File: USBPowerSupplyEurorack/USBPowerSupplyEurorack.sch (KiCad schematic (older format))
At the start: 19 parts, among them J1 1734366-1, J2 10129381-910001BLF, Q1 Q_PMOS_GSD

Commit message: added footprints with LCSC components
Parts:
- removed L1: 744235601, 744235601, symbol 744235601:744235601
- added L1: ACM4520V-901-2P-T, eec2:TDK-ACM4520V-901-2P-T-0, symbol eec2:ACM4520V-901-2P-T
- C1: footprint (none) -> Capacitor_SMD:C_Elec_8x10.2
- C2: footprint (none) -> Capacitor_SMD:C_1210_3225Metric
- C3, C4: footprint (none) -> Capacitor_SMD:C_1206_3216Metric
- C5, C6: footprint (none) -> Capacitor_SMD:C_Elec_4x5.4
- C7: footprint (none) -> Capacitor_SMD:C_Elec_6.3x5.8
- D2: value P4SMAJ15CA -> SMAJ5.0CA; footprint (none) -> digikey-footprints:DO-214AC
- D3, D4: footprint Diode_THT:D_DO-41_SOD81_P10.16mm_Horizontal -> Diode_SMD:D_SOD-123F
- F1: value 1812L110_16DR -> 1812L110; footprint FUSC4632X125N -> 1812L110_16DR:FUSC4632X125N; Description PTC Resettable Fuse 1.1A(hold) 1.95A(trip) 16VDC 100A 0.8W 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 -> PTC Resettable Fuse 1.1A(hold) 1.95A(trip) 8VDC 100A 0.8W 0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
- J2: footprint HDRV10W67P254_2X5_1270X483X858P -> 10129381-910001BLF:HDRV10W67P254_2X5_1270X483X858P
- R1: value 100 -> 510; footprint (none) -> Resistor_SMD:R_0612_1632Metric
- S1: footprint LP4OA1PBCTR -> LP4OA1PBCTR:LP4OA1PBCTR
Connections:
- net +12V: now also S1.L1 (A_RED)
- net +5V: now also L1.2; no longer R1.2, S1.L1 (A_RED)
- net +Vin: now also L1.4
- net -Vin: now also L1.3
- net 0V: now also R1.2
- net at C1.1, C2.1, C7.1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: now also L1.1
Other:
- moved on the sheet: C1, C2, C7, D2, Q1

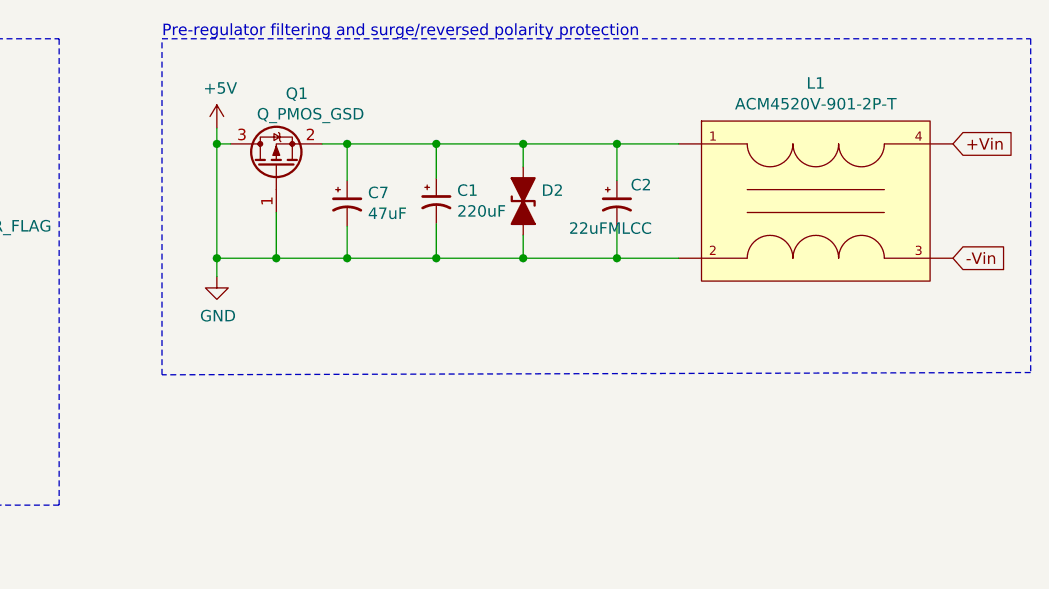
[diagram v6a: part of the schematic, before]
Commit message: changed TVS symbol as footprint was not valid
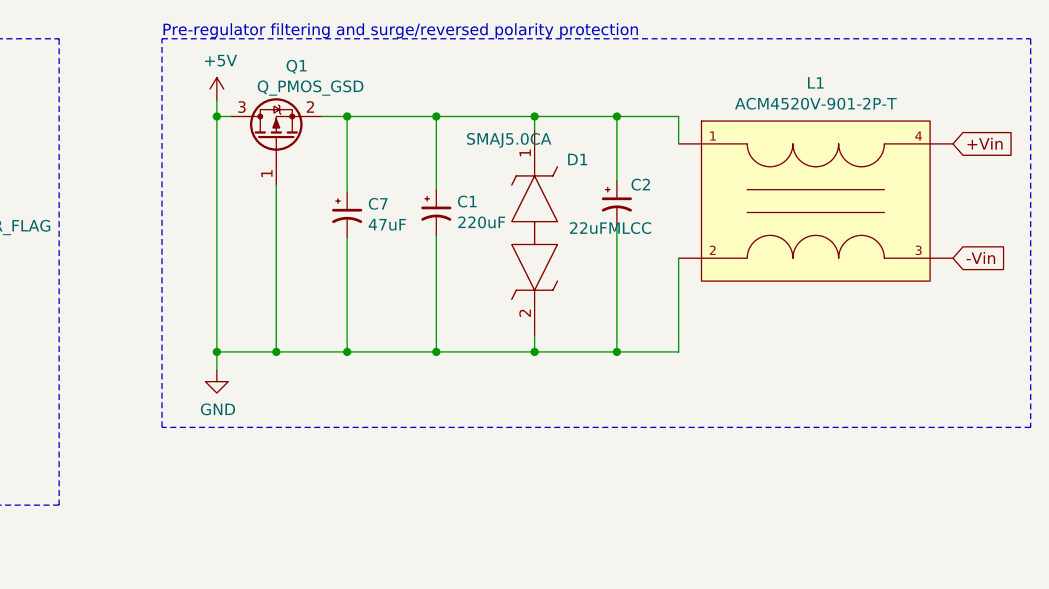
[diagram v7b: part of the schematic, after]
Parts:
- removed D2: SMAJ5.0CA, digikey-footprints:DO-214AC, symbol Device:D_TVS_ALT
- added D1: SMAJ5.0CA, DIONM5026X229N, symbol SMAJ5.0CA:SMAJ5.0CA
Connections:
- net +5V: now also D1.2
- net at C1.1, C2.1, C7.1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: now also D1.1
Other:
- moved on the sheet: C1, C7, Q1
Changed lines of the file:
@@
 L Device:CP1_Small C1
 U 1 1 5FE096E1
-P 8010 1720
-F 0 "C1" H 8101 1766 50  0000 L CNN
-F 1 "220uF" H 8101 1675 50  0000 L CNN
-F 2 "Capacitor_SMD:C_Elec_8x10.2" H 8010 1720 50  0001 C CNN
-F 3 "~" H 8010 1720 50  0001 C CNN
-	1    8010 1720
-	1    0    0    -1
-$EndComp
-$Comp
-L Device:D_TVS_ALT D2
-U 1 1 5FE0A48F
-P 8390 1720
-F 0 "D2" V 8344 1800 50  0000 L CNN
-F 1 "SMAJ5.0CA" V 8435 1800 50  0001 L CNN
-F 2 "digikey-footprints:DO-214AC" H 8390 1720 50  0001 C CNN
-F 3 "~" H 8390 1720 50  0001 C CNN
-	1    8390 1720
-	0    1    1    0
+P 8010 1770
+F 0 "C1" H 8101 1816 50  0000 L CNN
+F 1 "220uF" H 8101 1725 50  0000 L CNN
+F 2 "Capacitor_SMD:C_Elec_8x10.2" H 8010 1770 50  0001 C CNN
+F 3 "~" H 8010 1770 50  0001 C CNN
+	1    8010 1770
+	1    0    0    -1
 $EndComp
 $Comp
@@
 L power:+5V #PWR0106
 U 1 1 5FE2FAE8
-P 7050 1400
-F 0 "#PWR0106" H 7050 1250 50  0001 C CNN
-F 1 "+5V" H 7065 1573 50  0000 C CNN
-F 2 "" H 7050 1400 50  0001 C CNN
-F 3 "" H 7050 1400 50  0001 C CNN
-	1    7050 1400
+P 7050 1280
+F 0 "#PWR0106" H 7050 1130 50  0001 C CNN
+F 1 "+5V" H 7065 1453 50  0000 C CNN
+F 2 "" H 7050 1280 50  0001 C CNN
+F 3 "" H 7050 1280 50  0001 C CNN
+	1    7050 1280
 	1    0    0    -1
 $EndComp
@@
 $EndComp
 Wire Wire Line
-	8800 1830 8800 1970
-Wire Wire Line
-	8800 1630 8800 1470
-Wire Wire Line
-	8390 1570 8390 1470
-Wire Wire Line
-	8390 1470 8800 1470
-Wire Wire Line
-	8390 1870 8390 1970
-Wire Wire Line
-	8390 1970 8800 1970
-Wire Wire Line
-	8010 1620 8010 1470
-Wire Wire Line
-	8010 1470 8390 1470
-Connection ~ 8390 1470
-Wire Wire Line
-	8010 1820 8010 1970
-Wire Wire Line
-	8010 1970 8390 1970
-Connection ~ 8390 1970
+	8010 1670 8010 1350
+Wire Wire Line
+	8010 1870 8010 2380
 $Comp
 L power:GND #PWR0107
 U 1 1 5FE34916
-P 7050 2050
-F 0 "#PWR0107" H 7050 1800 50  0001 C CNN
-F 1 "GND" H 7055 1877 50  0000 C CNN
-F 2 "" H 7050 2050 50  0001 C CNN
-F 3 "" H 7050 2050 50  0001 C CNN
-	1    7050 2050
-	1    0    0    -1
-$EndComp
-Connection ~ 8010 1970
+P 7050 2460
+F 0 "#PWR0107" H 7050 2210 50  0001 C CNN
+F 1 "GND" H 7055 2287 50  0000 C CNN
+F 2 "" H 7050 2460 50  0001 C CNN
+F 3 "" H 7050 2460 50  0001 C CNN
+	1    7050 2460
+	1    0    0    -1
+$EndComp
+Connection ~ 8010 2380
 Wire Wire Line
 	2480 1490 2560 1490
 Wire Wire Line
 	2560 1490 2560 1440
-Connection ~ 8010 1470
+Connection ~ 8010 1350
 Text GLabel 10270 1470 2    50   Input ~ 0
 +Vin
@@
 L Device:CP1_Small C7
 U 1 1 5FE548E0
-P 7620 1730
-F 0 "C7" H 7711 1776 50  0000 L CNN
-F 1 "47uF" H 7711 1685 50  0000 L CNN
-F 2 "Capacitor_SMD:C_Elec_6.3x5.8" H 7620 1730 50  0001 C CNN
-F 3 "~" H 7620 1730 50  0001 C CNN
-	1    7620 1730
+P 7620 1780
+F 0 "C7" H 7711 1826 50  0000 L CNN
+F 1 "47uF" H 7711 1735 50  0000 L CNN
+F 2 "Capacitor_SMD:C_Elec_6.3x5.8" H 7620 1780 50  0001 C CNN
+F 3 "~" H 7620 1780 50  0001 C CNN
+	1    7620 1780
 	1    0    0    -1
 $EndComp
@@
 	4990 5650 4820 5650
 Wire Wire Line
-	8010 1470 7620 1470
-Wire Wire Line
-	7620 1470 7620 1630
-Wire Wire Line
-	7620 1830 7620 1970
-Wire Wire Line
-	7620 1970 8010 1970
-Connection ~ 7620 1970
-Connection ~ 7620 1470
+	8010 1350 7620 1350
+Wire Wire Line
+	7620 1350 7620 1680
+Wire Wire Line
+	7620 1880 7620 2380
+Wire Wire Line
+	7620 2380 8010 2380
+Connection ~ 7620 2380
+Connection ~ 7620 1350
 Wire Notes Line
 	6810 1010 10610 1010
 Wire Notes Line
-	10610 1010 10610 2470
-Wire Notes Line
-	10610 2470 6810 2480
-Wire Notes Line
-	6810 2480 6810 1010
+	10610 1010 10610 2710
+Wire Notes Line
+	10610 2710 6810 2710
+Wire Notes Line
+	6810 2710 6810 1010
 Text Notes 6810 1010 0    50   ~ 0
 Pre-regulator filtering and surge/reversed polarity protection
@@
 L Device:Q_PMOS_GSD Q1
 U 1 1 5FE39F03
-P 7310 1570
-F 0 "Q1" V 7630 1480 50  0000 C CNN
-F 1 "Q_PMOS_GSD" V 7540 1420 50  0000 C CNN
-F 2 "digikey-footprints:SOT-23-3" H 7510 1670 50  0001 C CNN
-F 3 "https://www.mouser.fr/datasheet/2/916/PMV240SP-1919536.pdf" H 7310 1570 50  0001 C CNN
-	1    7310 1570
+P 7310 1450
+F 0 "Q1" V 7630 1360 50  0000 C CNN
+F 1 "Q_PMOS_GSD" V 7540 1300 50  0000 C CNN
+F 2 "digikey-footprints:SOT-23-3" H 7510 1550 50  0001 C CNN
+F 3 "https://www.mouser.fr/datasheet/2/916/PMV240SP-1919536.pdf" H 7310 1450 50  0001 C CNN
+	1    7310 1450
 	0    -1   -1   0
 $EndComp
 Wire Wire Line
-	7620 1470 7510 1470
-Wire Wire Line
-	7310 1770 7310 1970
-Wire Wire Line
-	7310 1970 7620 1970
-Wire Wire Line
-	7110 1470 7050 1470
-Wire Wire Line
-	7050 1470 7050 1970
-Wire Wire Line
-	7050 1970 7310 1970
-Connection ~ 7310 1970
-Wire Wire Line
-	7050 1400 7050 1470
-Connection ~ 7050 1470
-Wire Wire Line
-	7050 2050 7050 1970
-Connection ~ 7050 1970
+	7620 1350 7510 1350
+Wire Wire Line
+	7310 1650 7310 2380
+Wire Wire Line
+	7310 2380 7620 2380
+Wire Wire Line
+	7110 1350 7050 1350
+Wire Wire Line
+	7050 1350 7050 2380
+Wire Wire Line
+	7050 2380 7310 2380
+Connection ~ 7310 2380
+Wire Wire Line
+	7050 1280 7050 1350
+Connection ~ 7050 1350
+Wire Wire Line
+	7050 2460 7050 2380
+Connection ~ 7050 2380
 $Comp
 L power:PWR_FLAG #FLG0102
@@
 	1    0    0    -1
 $EndComp
-Wire Wire Line
-	8800 1470 9070 1470
-Connection ~ 8800 1470
-Wire Wire Line
-	8800 1970 9070 1970
-Connection ~ 8800 1970
+$Comp
+L SMAJ5.0CA:SMAJ5.0CA D1
+U 1 1 5FE50B9A
+P 8440 1410
+F 0 "D1" V 8570 1550 50  0000 L CNN
+F 1 "SMAJ5.0CA" V 8480 1110 50  0000 L CNN
+F 2 "DIONM5026X229N" H 9040 1560 50  0001 L BNN
+F 3 "http://www.littelfuse.com/~/media/electronics/datasheets/tvs_diodes/littelfuse_tvs_diode_smaj_datasheet.pdf.pdf" H 9040 1460 50  0001 L BNN
+F 4 "Littelfuse SMAJ5.0CA Bi-Directional TVS Diode, 400W peak, 2-Pin DO-214AC" H 9040 1360 50  0001 L BNN "Description"
+F 5 "2.29" H 9040 1260 50  0001 L BNN "Height"
+F 6 "LITTELFUSE" H 9040 1160 50  0001 L BNN "Manufacturer_Name"
+F 7 "SMAJ5.0CA" H 9040 1060 50  0001 L BNN "Manufacturer_Part_Number"
+F 8 "576-SMAJ5.0CA" H 9040 960 50  0001 L BNN "Mouser Part Number"
+F 9 "https://www.mouser.co.uk/ProductDetail/Littelfuse/SMAJ50CA?qs=JJML70Qc14u8hb22RFwTwA%3D%3D" H 9040 860 50  0001 L BNN "Mouser Price/Stock"
+F 10 "SMAJ5.0CA" H 9040 760 50  0001 L BNN "Arrow Part Number"
+F 11 "https://www.arrow.com/en/products/smaj5.0ca/littelfuse" H 9040 660 50  0001 L BNN "Arrow Price/Stock"
+	1    8440 1410
+	0    1    1    0
+$EndComp
+Wire Wire Line
+	8440 1350 8440 1410
+Wire Wire Line
+	8010 1350 8440 1350
+Wire Wire Line
+	8440 1350 8800 1350
+Wire Wire Line
+	8800 1350 8800 1630
+Connection ~ 8440 1350
+Wire Wire Line
+	8800 1350 9070 1350
+Wire Wire Line
+	9070 1350 9070 1470
+Connection ~ 8800 1350
+Wire Wire Line
+	9070 2380 9070 1970
+Wire Wire Line
+	8800 1830 8800 2380
+Wire Wire Line
+	8010 2380 8440 2380
+Connection ~ 8800 2380
+Wire Wire Line
+	8800 2380 9070 2380
+Wire Wire Line
+	8440 2310 8440 2380
+Connection ~ 8440 2380
+Wire Wire Line
+	8440 2380 8800 2380
 $EndSCHEMATC

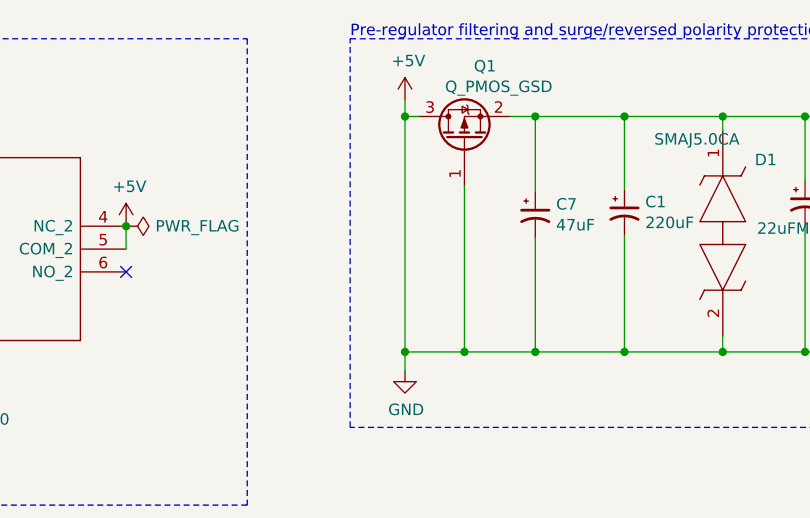
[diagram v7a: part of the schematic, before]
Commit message: placed components on the PCB
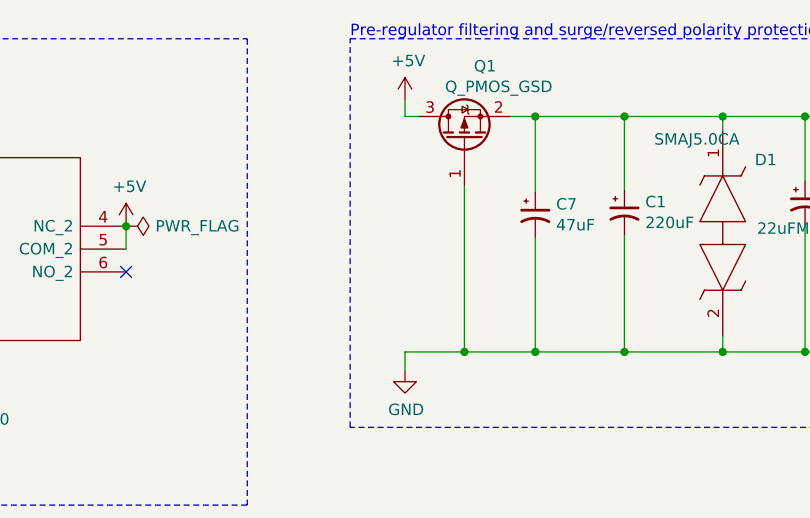
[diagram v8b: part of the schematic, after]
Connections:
- net +5V: no longer C1.2, C2.2, C7.2, D1.2, J1.4 (P4), L1.2, Q1.1 (G)
- new net GND: C1.2, C2.2, C7.2, D1.2, J1.4 (P4), L1.2, Q1.1 (G)
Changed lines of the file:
@@
 	7110 1350 7050 1350
-Wire Wire Line
-	7050 1350 7050 2380
 Wire Wire Line
 	7050 2380 7310 2380
@@
 Wire Wire Line
 	7050 1280 7050 1350
-Connection ~ 7050 1350
 Wire Wire Line
 	7050 2460 7050 2380
-Connection ~ 7050 2380
 $Comp
 L power:PWR_FLAG #FLG0102
